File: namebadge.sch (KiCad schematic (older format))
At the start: 7 parts, among them IC1 SN74AHCT125N, J1 Barrel_Jack, SW1 SW_Push, U1 Pico

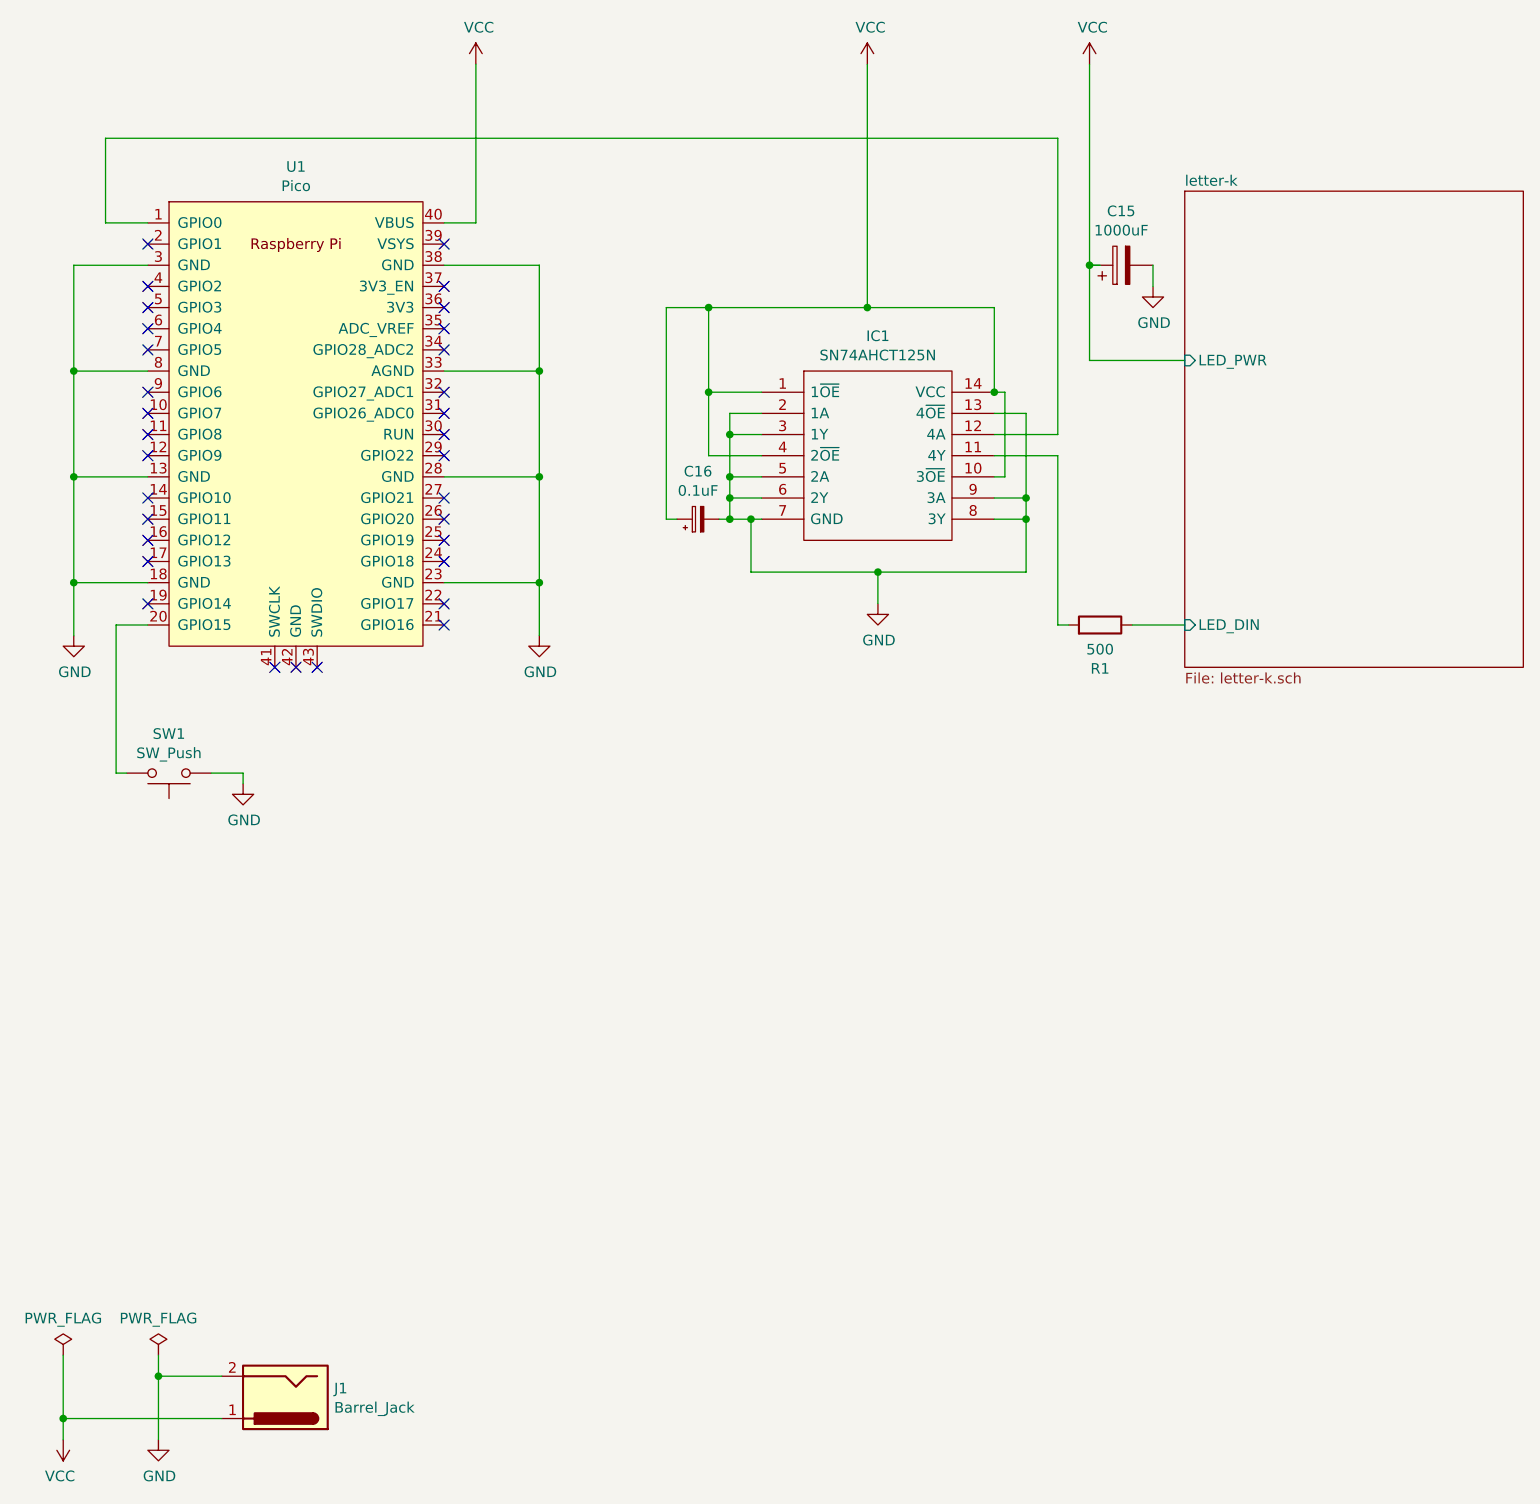
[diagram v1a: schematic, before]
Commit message: Adds a Schottky on the DC input and moves it to VSYS, not VBUS.
Fixes #4.
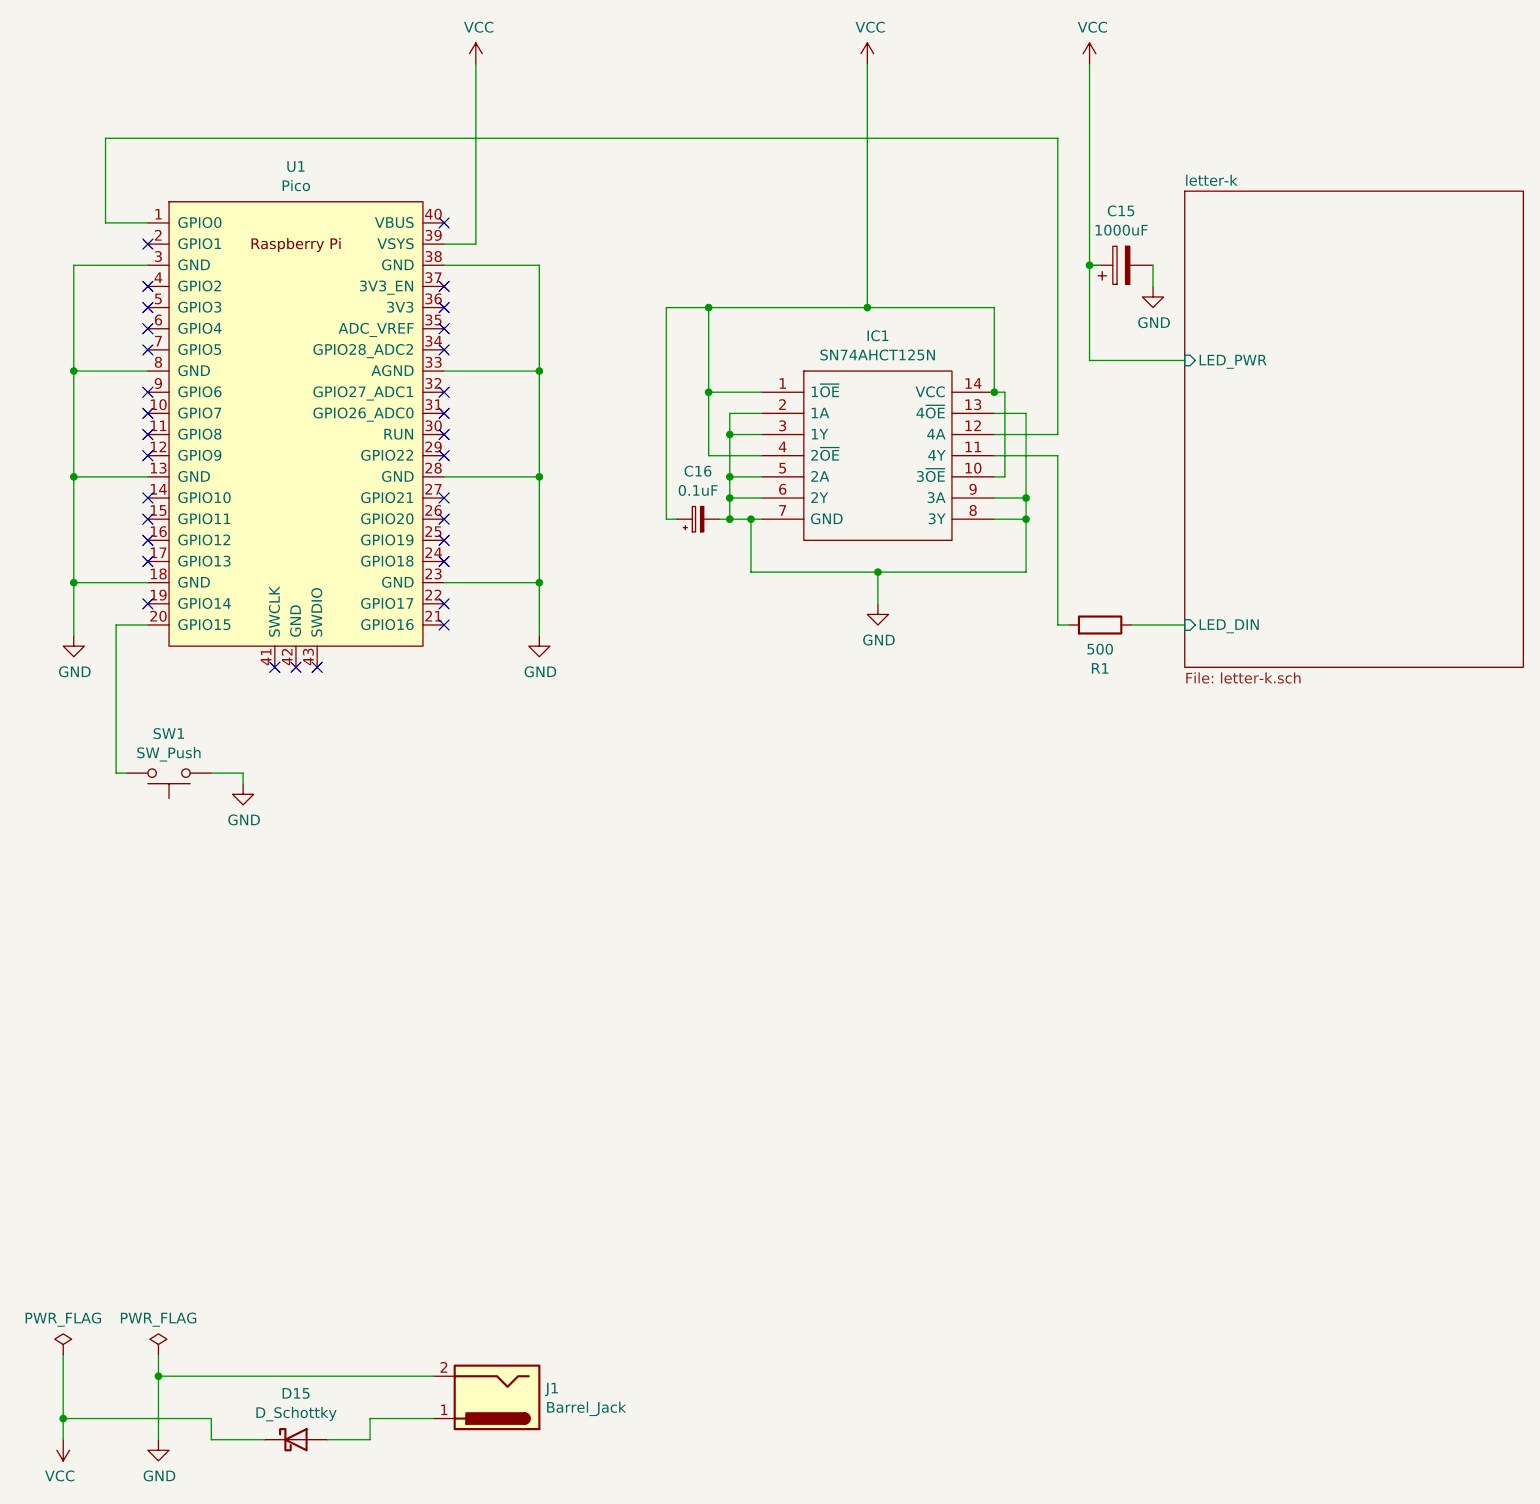
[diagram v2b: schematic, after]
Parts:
- added D15: D_Schottky, Diode_THT:D_DO-41_SOD81_P10.16mm_Horizontal, symbol Device:D_Schottky
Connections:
- net VCC: now also U1.39 (VSYS), D15.1 (K); no longer J1.1, U1.40 (VBUS)
- new net: D15.2 (A), J1.1
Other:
- moved on the sheet: J1
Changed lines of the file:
@@
 L Connector:Barrel_Jack J1
 U 1 1 6074B59D
-P 2050 7200
-F 0 "J1" H 1820 7158 50  0000 R CNN
-F 1 "Barrel_Jack" H 1820 7249 50  0000 R CNN
-F 2 "Connector_BarrelJack:BarrelJack_CUI_PJ-063AH_Horizontal" H 2100 7160 50  0001 C CNN
-F 3 "~" H 2100 7160 50  0001 C CNN
-	1    2050 7200
+P 3050 7200
+F 0 "J1" H 2820 7158 50  0000 R CNN
+F 1 "Barrel_Jack" H 2820 7249 50  0000 R CNN
+F 2 "Connector_BarrelJack:BarrelJack_CUI_PJ-063AH_Horizontal" H 3100 7160 50  0001 C CNN
+F 3 "~" H 3100 7160 50  0001 C CNN
+	1    3050 7200
 	-1   0    0    1
 $EndComp
@@
 	1450 7000 1450 7100
 Wire Wire Line
-	1000 7000 1000 7300
-Wire Wire Line
-	1750 7300 1000 7300
-Connection ~ 1000 7300
-Wire Wire Line
-	1000 7300 1000 7400
-Wire Wire Line
-	1750 7100 1450 7100
+	2750 7100 1450 7100
 Connection ~ 1450 7100
 Wire Wire Line
@@
 Wire Wire Line
 	1850 4250 1850 4300
-NoConn ~ 2800 1750
 Wire Wire Line
 	4800 900  4800 2050
@@
 	3250 3600 3250 3350
 Connection ~ 3250 3350
-Wire Wire Line
-	2950 900  2950 1650
-Wire Wire Line
-	2950 1650 2800 1650
 $Comp
 L power:VCC #PWR0121
@@
 Wire Wire Line
 	5550 3050 5550 3300
+Wire Wire Line
+	2950 1750 2800 1750
+Wire Wire Line
+	2950 900  2950 1750
+NoConn ~ 2800 1650
+Wire Wire Line
+	1000 7000 1000 7300
+$Comp
+L Device:D_Schottky D15
+U 1 1 6055D58C
+P 2100 7400
+F 0 "D15" H 2100 7617 50  0000 C CNN
+F 1 "D_Schottky" H 2100 7526 50  0000 C CNN
+F 2 "Diode_THT:D_DO-41_SOD81_P10.16mm_Horizontal" H 2100 7400 50  0001 C CNN
+F 3 "~" H 2100 7400 50  0001 C CNN
+	1    2100 7400
+	1    0    0    -1
+$EndComp
+Connection ~ 1000 7300
+Wire Wire Line
+	1000 7300 1000 7400
+Wire Wire Line
+	1000 7300 1700 7300
+Wire Wire Line
+	1700 7300 1700 7400
+Wire Wire Line
+	1700 7400 1950 7400
+Wire Wire Line
+	2250 7400 2450 7400
+Wire Wire Line
+	2450 7400 2450 7300
+Wire Wire Line
+	2450 7300 2750 7300
 $EndSCHEMATC
